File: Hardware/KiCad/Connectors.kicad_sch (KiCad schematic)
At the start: 48 parts

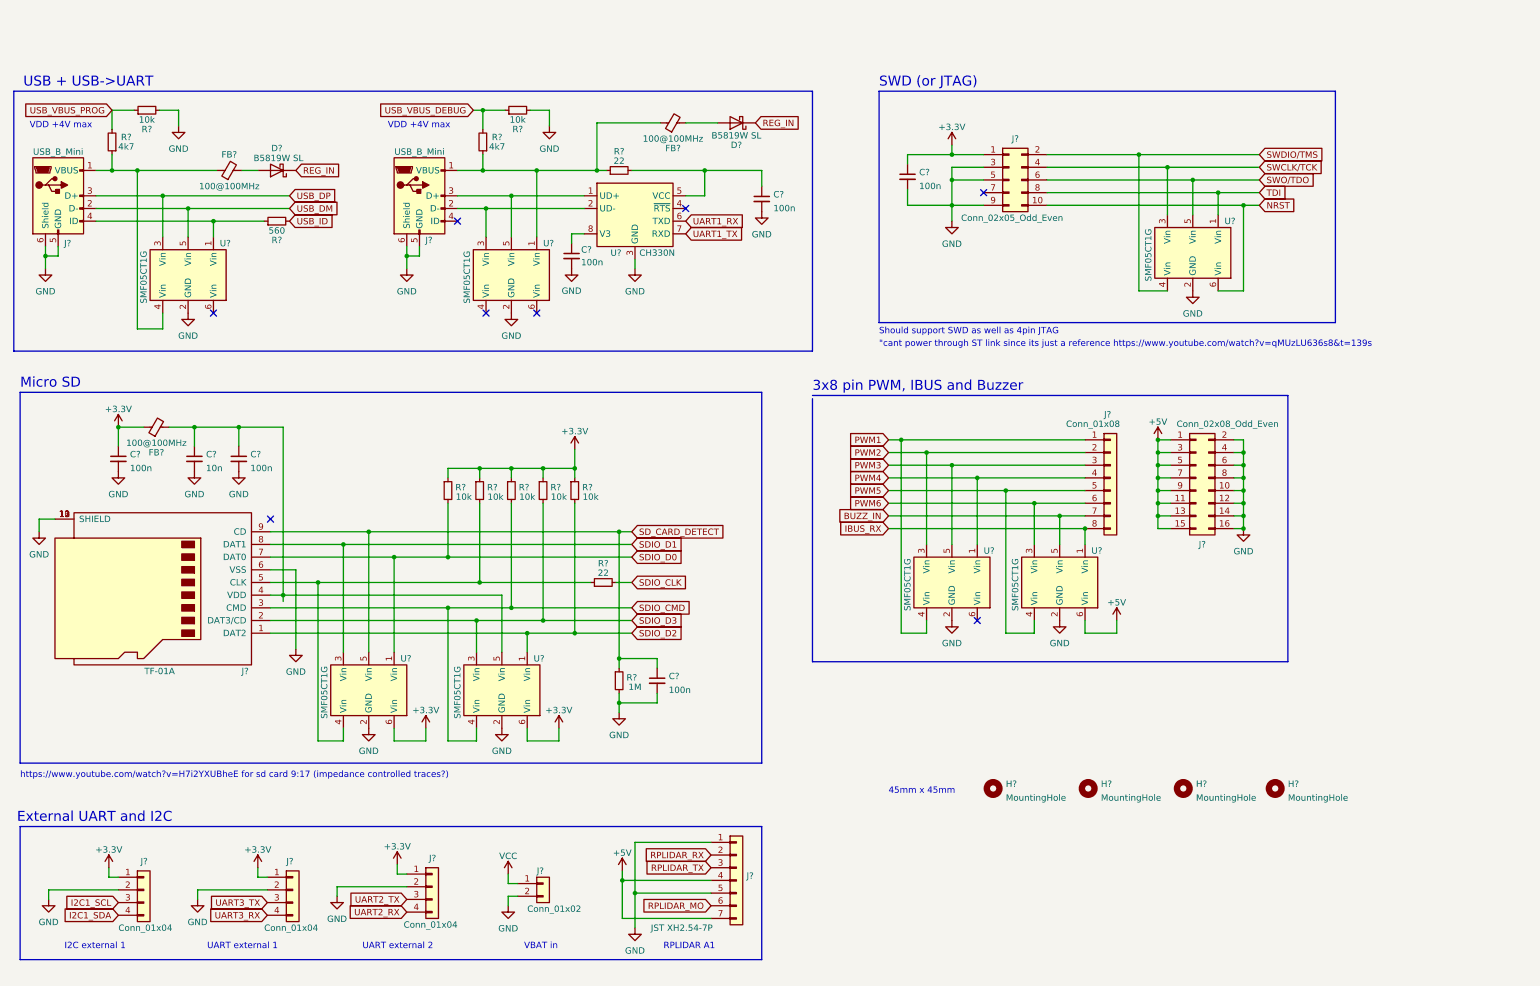
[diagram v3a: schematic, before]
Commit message: Added pullups, testpoints and more pin definitions
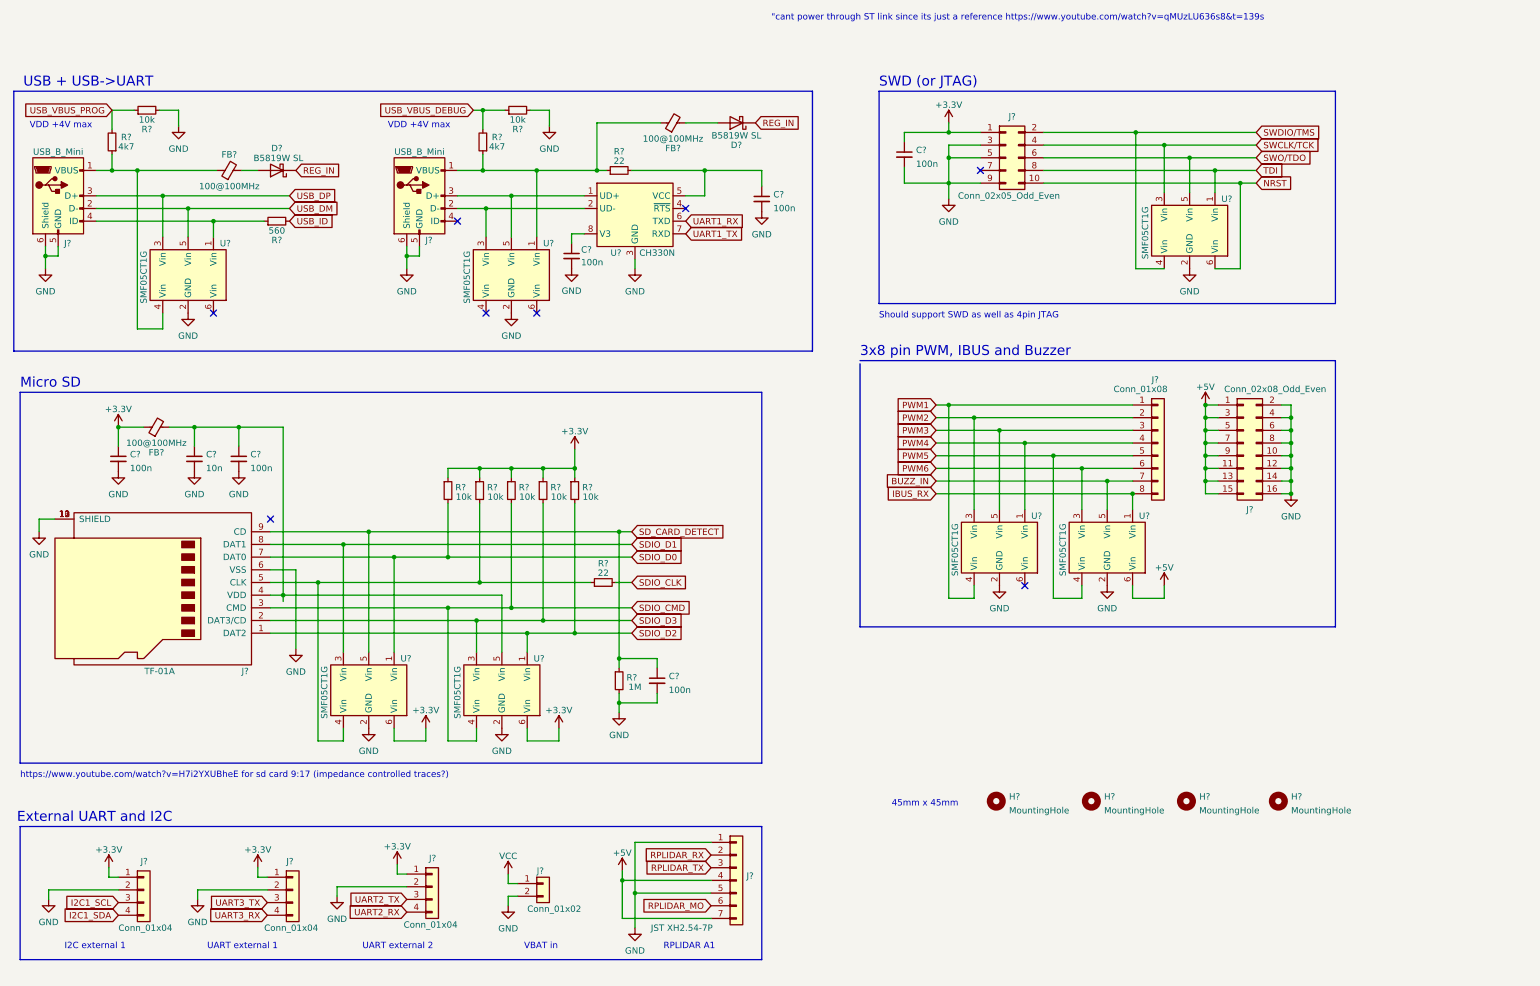
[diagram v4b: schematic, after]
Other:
- moved on the sheet: C?, H?, J?, U?

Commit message: Added a connector for 4 external LEDs
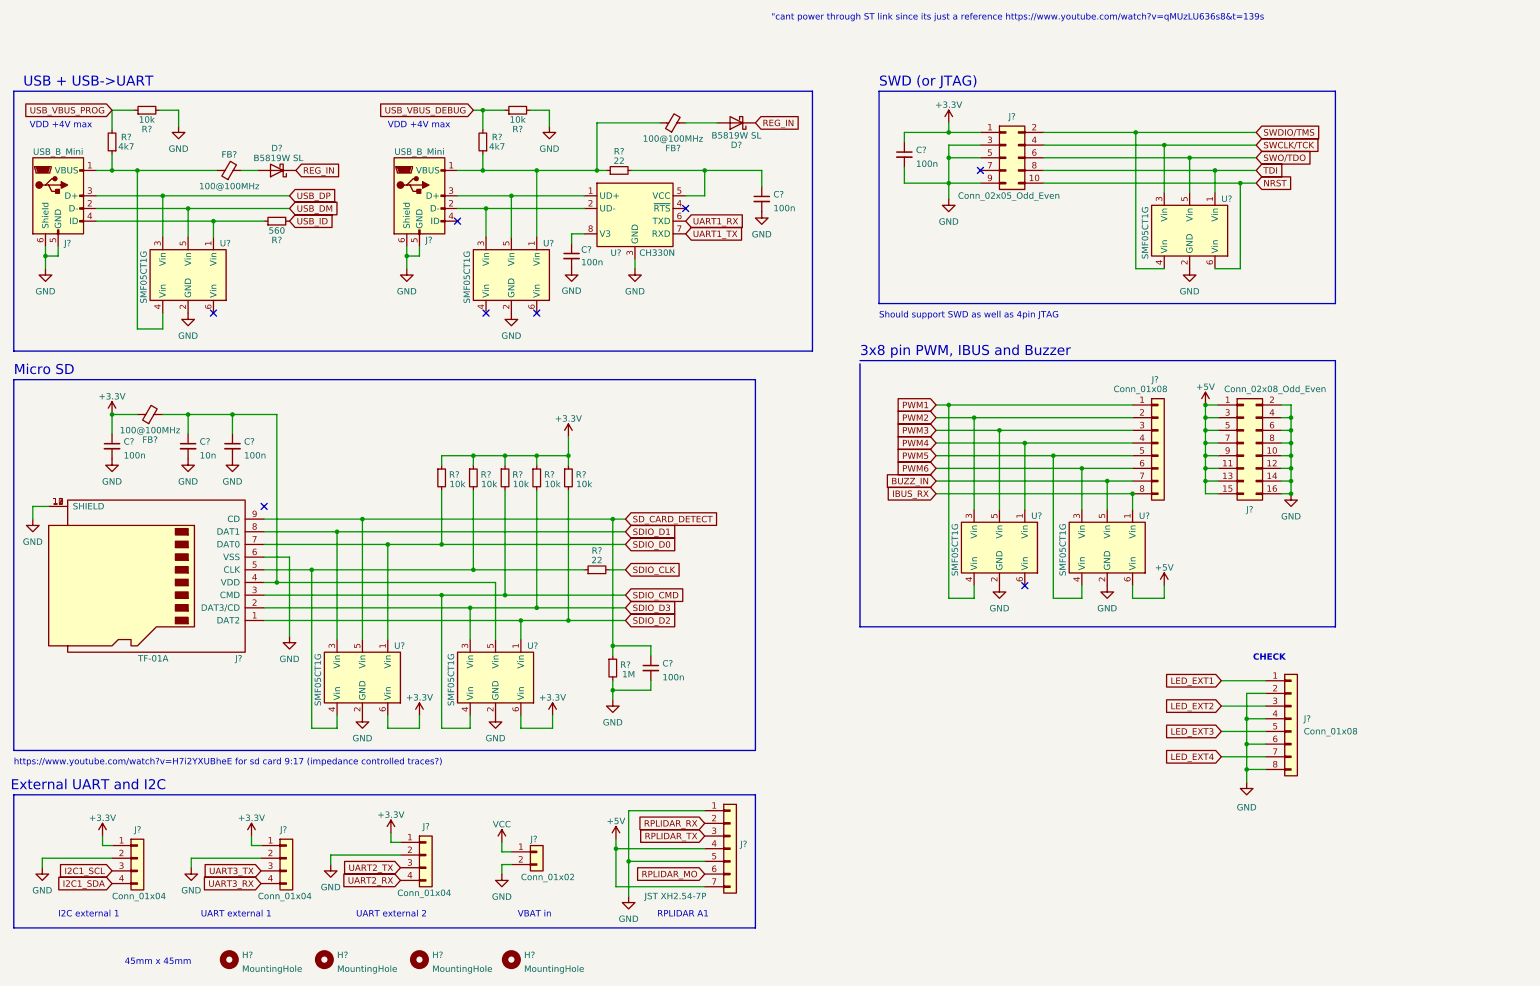
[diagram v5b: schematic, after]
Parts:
- added J?: Conn_01x08, symbol Connector_Generic:Conn_01x08
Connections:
- net GND: now also J?.2 (Pin_2), J?.4 (Pin_4), J?.6 (Pin_6), J?.8 (Pin_8)
- new net LED_EXT1: J?.1 (Pin_1)
- new net LED_EXT2: J?.3 (Pin_3)
- new net LED_EXT3: J?.5 (Pin_5)
- new net LED_EXT4: J?.7 (Pin_7)
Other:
- note added: "CHECK"
- moved on the sheet: C?, FB?, H?, J?, R?, U?
